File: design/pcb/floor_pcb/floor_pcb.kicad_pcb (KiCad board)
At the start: 2 copper layers, 75 x 222 mm, 11 parts, among them J1 Conn_01x10_Male, J10 shock_grid, J11 shock_grid, J2 Conn_01x10_Male, J3 DB25_Male, J4 shock_grid, J5 shock_grid, J6 shock_grid, J7 shock_grid, J8 shock_grid, J9 shock_grid

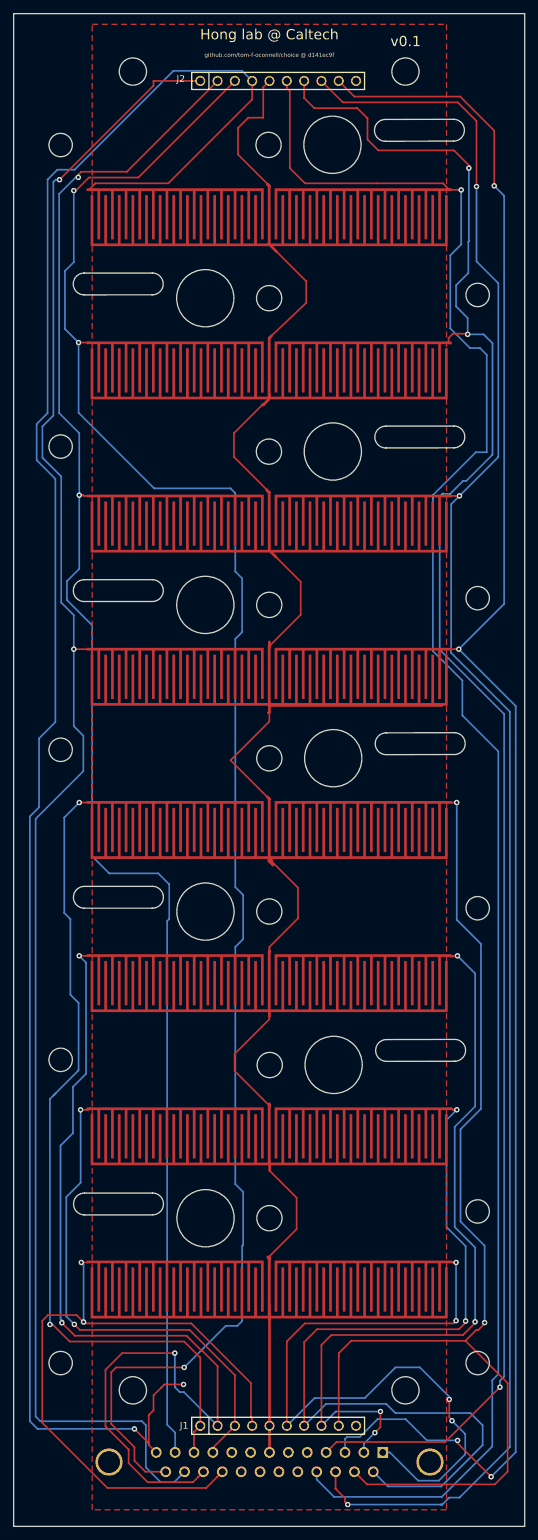
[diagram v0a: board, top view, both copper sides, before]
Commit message: Made second round of floor pcb gerbers, still before ordering because first quotes were really expensive. Needed to add soldermask, but still having some slight issues (can't make clearance more than custom polygon pad it seems, not add polygon on top of it in GUI). Tweaked some part values for another order. Regenerated floor electrodes with sorta fixed soldermask.
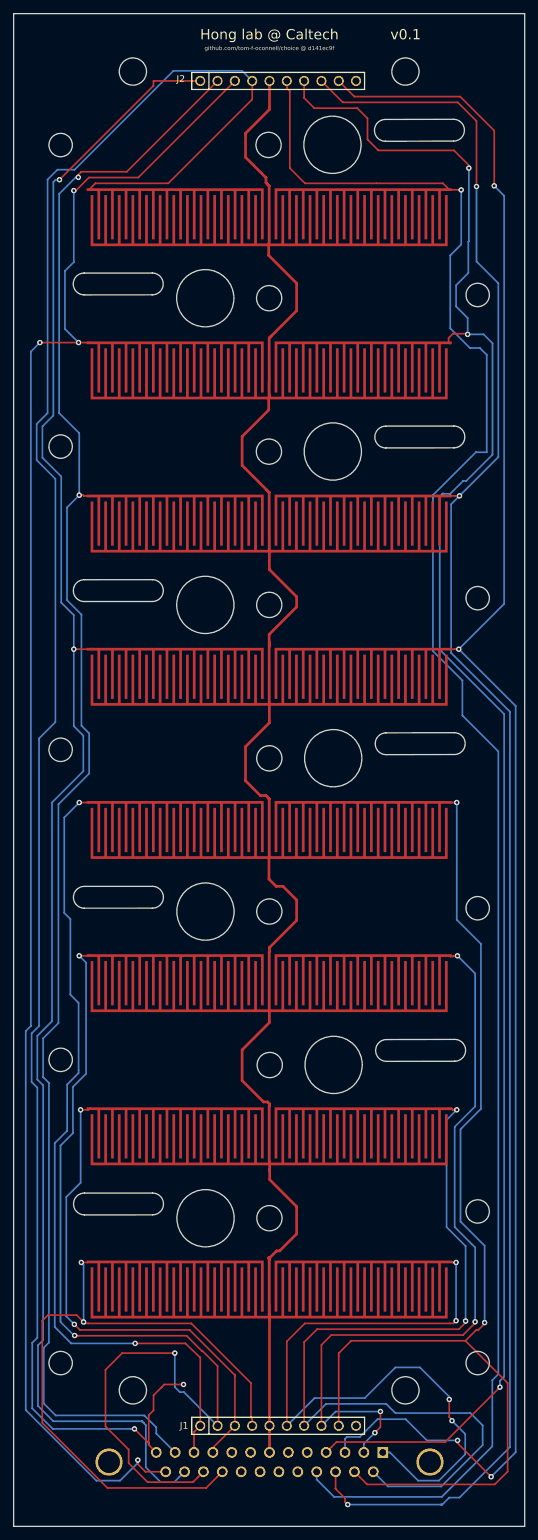
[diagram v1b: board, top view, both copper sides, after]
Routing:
- net /HV: track 282.3 -> 245.7 mm
- net /F3: track 259.8 -> 246.4 mm, vias 3 -> 4
- net /F5: track 229.5 -> 238.9 mm
- net /F9: track 120.4 -> 119.2 mm
- net /F1: track 288.3 -> 287.4 mm
- removed copper zone on F.Cu, net /HV
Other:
- rule pad_to_mask_clearance: 0.2 -> 0.35
- board text added: "Be cautious with potential heat distributions, particularly if one chamber is shorted, considering this might affect the animal's behavior."
- board text added: "Board should be 1/16" thick (1.5875 mm) Might benefit from some kind of gold finish, to lower contact resistance and prevent changes in resistance due to oxidation. Hard gold seems more well suited. Could probably withstand more cleaning cycles. ENIG may be fine."
- board text removed: "Be cautious with heat in particularly the back copper traces, in cases where the heat from a shorted chamber might affect the behavior of a fly in another chamber. Maybe fix if redesigning, though might need to make wider."
- board text removed: "Board should be 1/16" thick (1.5875 mm)"
